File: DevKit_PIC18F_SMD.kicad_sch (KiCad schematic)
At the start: 25 parts, among them J1 PIC_ICSP_ICD, J2 USB_B_Mini, J5 RIGHT_PORT, J6 LEFT_PORT, SW1 C318938, X1 16MHz

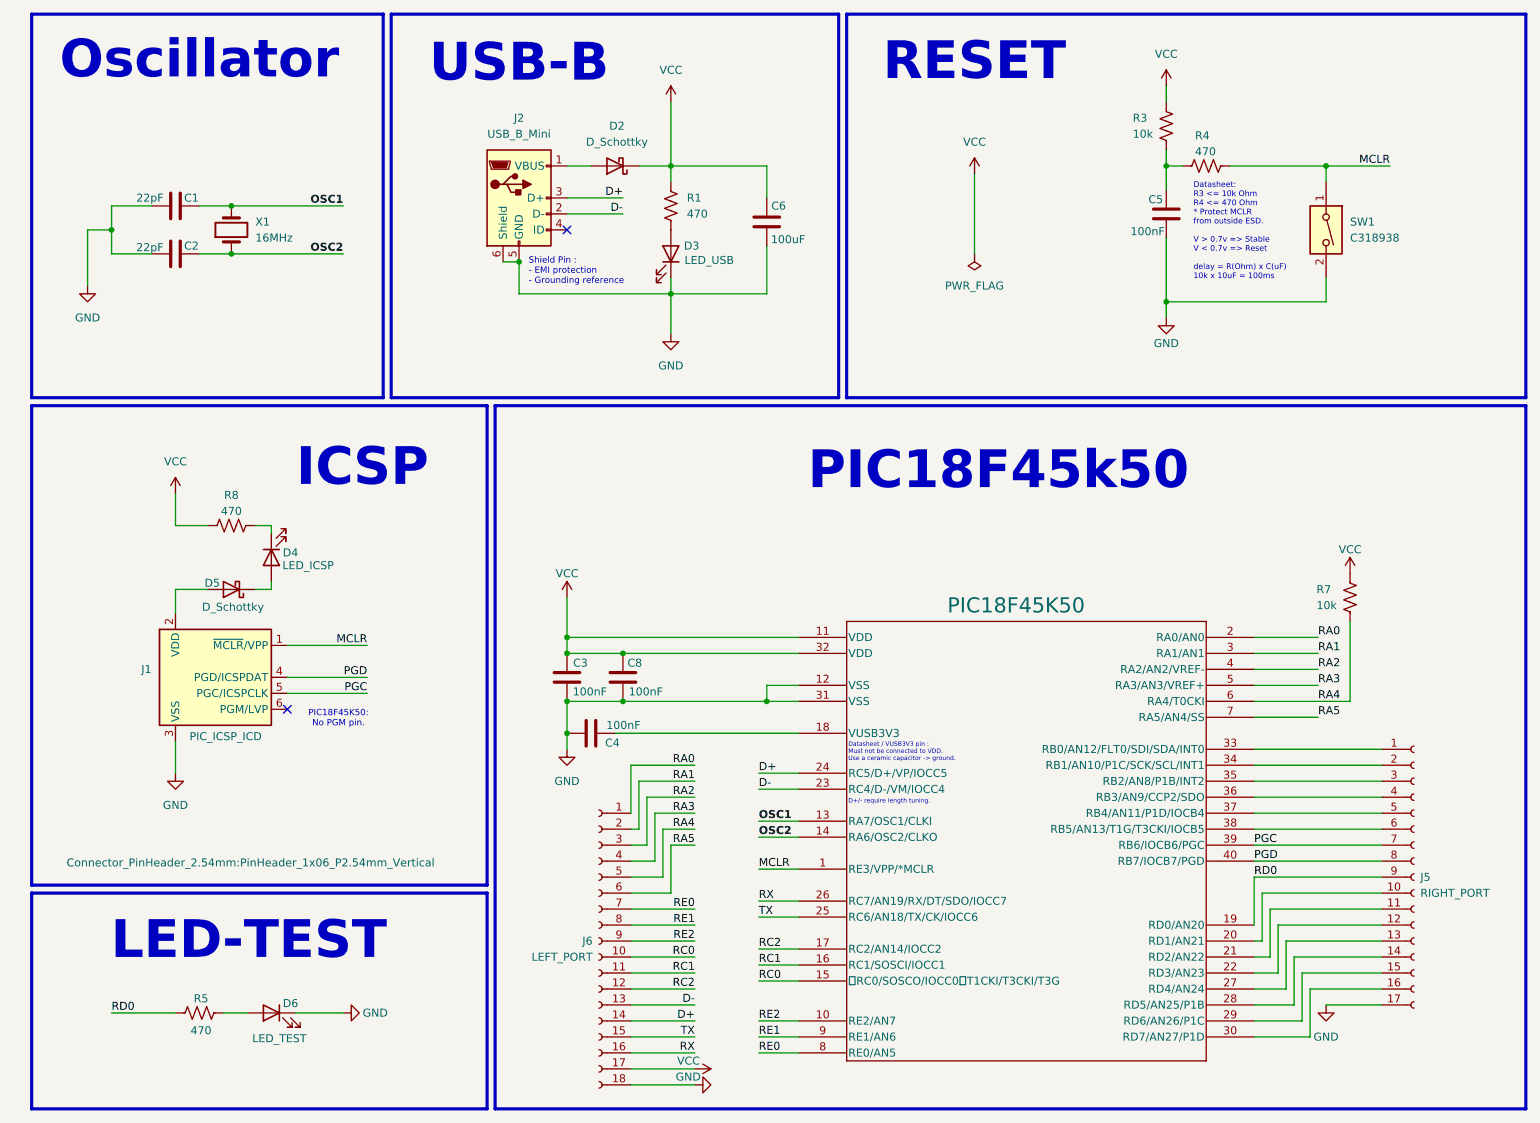
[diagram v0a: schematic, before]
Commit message: Fix Reset Button, ICSP... etc.
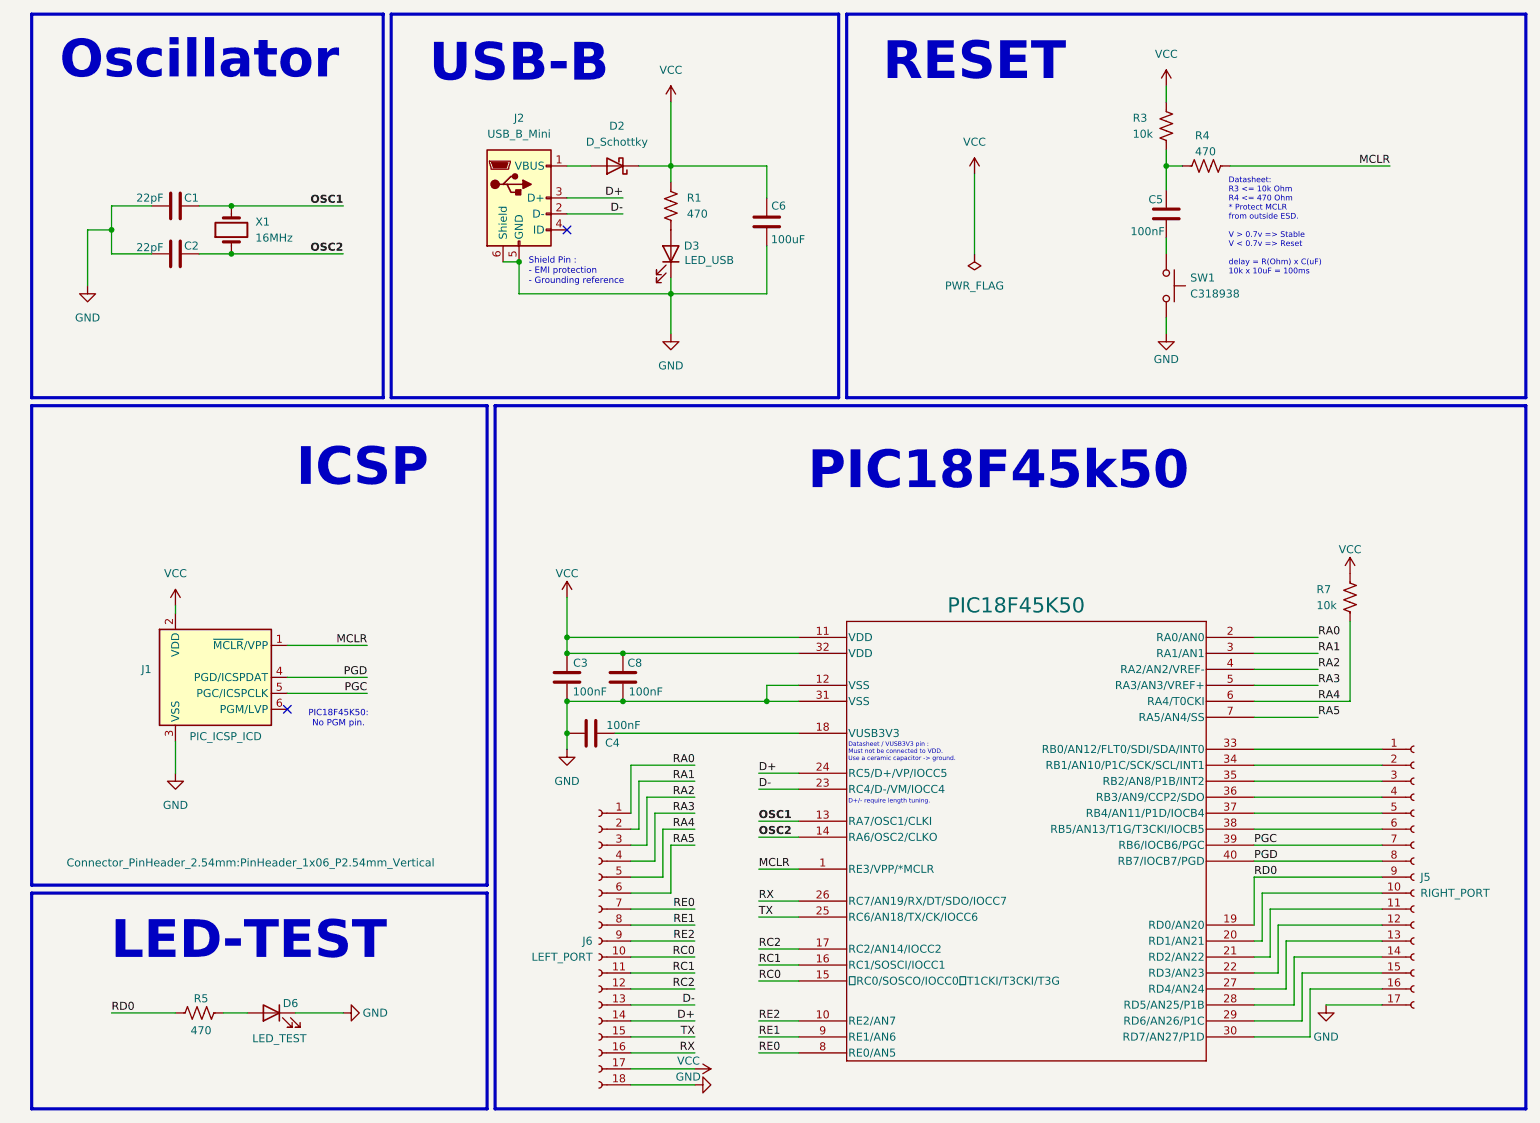
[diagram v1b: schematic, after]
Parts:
- removed D4: LED_ICSP, LED_SMD:LED_0805_2012Metric, symbol Device:LED
- removed D5: D_Schottky, Diode_SMD:D_0603_1608Metric, symbol Device:D_Schottky
- removed R8: 470, Resistor_SMD:R_0805_2012Metric, symbol Device:R_US
- SW1: symbol Switch:SW_DIP_x01 -> Switch:SW_Push
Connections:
- net GND: no longer C5.1
- net MCLR: no longer SW1.1
- net VCC: now also J1.2 (VDD)
- new net: C5.1, SW1.1
